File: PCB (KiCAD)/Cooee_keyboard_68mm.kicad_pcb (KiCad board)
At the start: 2 copper layers, 67.9 x 51 mm, 99 parts, among them J1 Conn_01x15_Pin

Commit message: finished routing new smaller keyboard
finished routing new smaller keyboard
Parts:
- removed H1: MountingHole, MountingHole:MountingHole_3.2mm_M3_ISO7380_Pad
- H4, H5: footprint MountingHole:MountingHole_3.2mm_M3_ISO7380_Pad -> MountingHole:MountingHole_3.2mm_M3
- moved D22 6.88 mm to (160.5, 120.5), turned to -90 degrees
- moved D93 6.28 mm to (161.1, 115.7), turned to -90 degrees
- moved J1 6.03 mm to (167.7, 73.2)
- moved D54 4.81 mm to (176.3, 111.8), turned to -90 degrees
- moved D18 4.56 mm to (157.8, 118.4)
- moved H4 4.52 mm to (177.2, 74.8)
- moved SWe7 3.32 mm to (171.0, 121.1)
- moved D28 3.27 mm to (170.4, 118.4)
- moved SWe13 2.74 mm to (157.0, 121.1)
- moved H5 2.58 mm to (121.8, 74.8)
- moved SWe2 1.84 mm to (163.8, 121.3), turned to 180 degrees
- moved SWe88 0.70 mm to (163.7, 115.0)
- moved H7 0.53 mm to (179.5, 119.0)
- moved D44 0.30 mm to (181.8, 89.4)
- moved SWe37 0.30 mm to (181.1, 86.8)
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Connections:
- D14 pad 1: COL2 -> COL3
- D17 pad 1: COL3 -> COL4
- D21 pad 1: COL4 -> COL5
- D22 pad 1: COL5 -> COL6
- D27 pad 1: COL6 -> COL7
- D28 pad 2: COL7 -> COL8
- D31 pad 1: COL7 -> COL8
- D39 pad 1: COL9 -> COL10
- D44 pad 1: COL9 -> COL10
- D5 pad 1: COL2 -> COL1
- D51 pad 1: COL8 -> COL2
- D52 pad 1: COL8 -> COL9
- D54 pad 1: COL8 -> COL10
- D7 pad 1: COL1 -> COL2
- D92 pad 1: COL5 -> COL6
- D93 pad 1: COL6 -> COL7
- J1 pad 1: ROW6 -> COL10
- J1 pad 2: ROW5 -> COL9
- J1 pad 3: ROW4 -> COL8
- J1 pad 4: ROW3 -> COL7
- J1 pad 5: ROW2 -> ROW5
- J1 pad 6: ROW1 -> ROW4
- J1 pad 7: COL9 -> ROW3
- J1 pad 8: COL8 -> ROW2
- J1 pad 9: COL7 -> ROW1
- SWe17 pad 1: ROW5 -> ROW4
- SWe2 pad 1: ROW6 -> ROW5
- SWe24 pad 1: ROW5 -> ROW4
- SWe29 pad 1: ROW2 -> ROW1
- SWe36 pad 1: ROW3 -> ROW2
- SWe37 pad 1: ROW6 -> ROW2
- SWe39 pad 1: ROW4 -> ROW3
- SWe47 pad 1: ROW4 -> ROW5
- SWe50 pad 1: ROW6 -> ROW5
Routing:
- net ROW5: track 0.00 -> 136.3 mm, vias 0 -> 1
- net ROW4: track 0.00 -> 103.9 mm, vias 0 -> 1
- net ROW3: track 0.00 -> 94.2 mm, vias 0 -> 1
- net ROW2: track 0.00 -> 89.4 mm, vias 0 -> 1
- net ROW1: track 0.00 -> 82.2 mm
- net COL6: track 0.00 -> 72.7 mm, vias 0 -> 5
- net COL8: track 0.00 -> 67.3 mm, vias 0 -> 5
- net COL5: track 0.00 -> 66.8 mm, vias 0 -> 5
- net COL1: track 0.00 -> 65.2 mm, vias 0 -> 5
- net COL9: track 0.00 -> 64.9 mm, vias 0 -> 5
- net COL2: track 0.00 -> 59.6 mm, vias 0 -> 5
- net COL10: track 0.00 -> 57.0 mm, vias 0 -> 3
- net COL7: track 0.00 -> 56.6 mm, vias 0 -> 5
- net COL4: track 0.00 -> 54.4 mm, vias 0 -> 4
- net COL3: track 0.00 -> 43.9 mm, vias 0 -> 4
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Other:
- board size 67.9 x 51 mm -> 66.8 x 51.8 mm

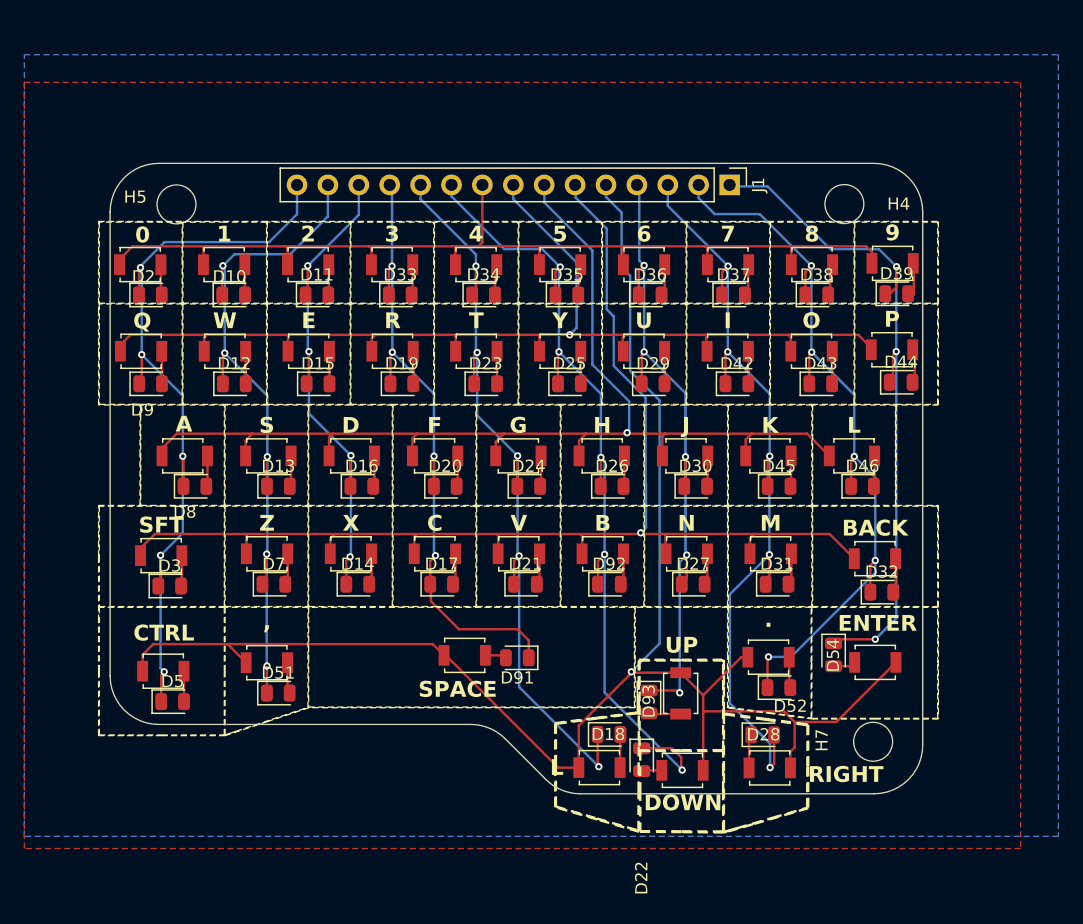
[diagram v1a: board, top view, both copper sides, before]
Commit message: finished keyboard at 67mm
started work on esp32 motherboard
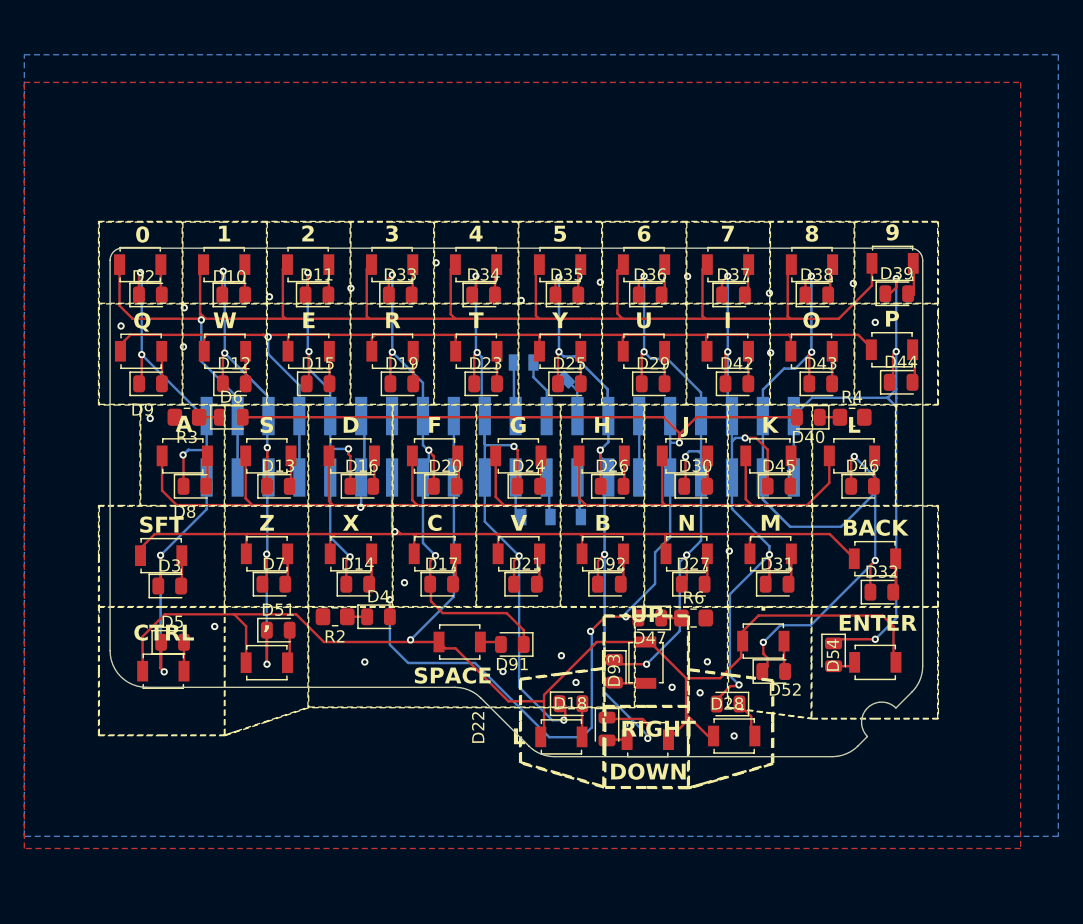
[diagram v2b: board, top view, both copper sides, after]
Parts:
- removed H4, H5, H7: MountingHole, MountingHole:MountingHole_3.2mm_M3
- added D4: SS24, Diode_SMD:D_0805_2012Metric, F.Cu at (138.9, 108.7)
- added D40: SS24, Diode_SMD:D_0805_2012Metric, F.Cu at (174.2, 92.3)
- added D47: SS24, Diode_SMD:D_0805_2012Metric, F.Cu at (161.2, 108.8)
- added D6: SS24, Diode_SMD:D_0805_2012Metric, F.Cu at (126.8, 92.3)
- added J2: Conn_01x01_Pin, USB4105-GF-A (1):Lil_Pad, B.Cu at (155.5, 100.5)
- added J3: Conn_01x01_Pin, USB4105-GF-A (1):Lil_Pad, B.Cu at (154.3, 89.2)
- added J4: Conn_01x01_Pin, USB4105-GF-A (1):Lil_Pad, B.Cu at (153.0, 100.5)
- added J5: Conn_01x01_Pin, USB4105-GF-A (1):Lil_Pad, B.Cu at (151.6, 87.8)
- added J6: Conn_01x01_Pin, USB4105-GF-A (1):Lil_Pad, B.Cu at (150.6, 100.5)
- added J7: Conn_01x01_Pin, USB4105-GF-A (1):Lil_Pad, B.Cu at (150.0, 87.8)
- added R2: R, Resistor_SMD:R_0805_2012Metric_Pad1.20x1.40mm_HandSolder, F.Cu at (135.3, 108.7)
- added R3: R, Resistor_SMD:R_0805_2012Metric_Pad1.20x1.40mm_HandSolder, F.Cu at (123.1, 92.3)
- added R4: R, Resistor_SMD:R_0805_2012Metric_Pad1.20x1.40mm_HandSolder, F.Cu at (177.8, 92.3)
- added R6: R, Resistor_SMD:R_0805_2012Metric_Pad1.20x1.40mm_HandSolder, F.Cu at (164.8, 108.8)
- J1: value Conn_01x15_Pin -> Conn_02x20_Counter_Clockwise; footprint Connector_PinHeader_2.54mm:PinHeader_1x15_P2.54mm_Vertical -> Connector_PinHeader_2.54mm:PinHeader_2x20_P2.54mm_Vertical_SMD; moved to B.Cu
- moved J1 28.6 mm to (148.9, 94.7)
- moved D51 5.17 mm to (130.6, 109.8)
- moved D5 4.88 mm to (121.9, 110.8)
- moved D18 4.02 mm to (154.7, 115.8)
- moved SWe13 4.02 mm to (153.9, 118.6)
- moved SWe7 3.93 mm to (168.1, 118.5), turned to 180 degrees
- moved D28 3.81 mm to (167.6, 115.9), turned to 180 degrees
- moved D22 3.81 mm to (157.7, 117.9)
- moved D93 3.81 mm to (158.3, 113.2)
- moved SWe2 3.81 mm to (161.0, 118.8)
- moved SWe88 3.81 mm to (160.9, 112.5)
- moved SWe48 1.39 mm to (170.5, 110.7)
- moved D52 1.39 mm to (171.4, 113.2)
- moved D91 1.17 mm to (149.9, 111.0)
- moved SWe86 1.17 mm to (145.5, 110.8)
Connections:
- J1 pad 1: COL10 -> COL1
- J1 pad 10: COL6 -> COL3
- J1 pad 11: COL5 -> ROW3
- J1 pad 12: COL4 -> ROW3
- J1 pad 13: COL3 -> ROW4
- J1 pad 14: COL2 -> ROW4
- J1 pad 15: COL1 -> COL4
- J1 pad 2: COL9 -> COL1
- J1 pad 3: COL8 -> ROW1
- J1 pad 4: COL7 -> ROW1
- J1 pad 5: ROW5 -> COL2
- J1 pad 6: ROW4 -> COL2
- J1 pad 7: ROW3 -> ROW2
- J1 pad 9: ROW1 -> COL3
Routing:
- net +3.3V: track 0.00 -> 104.5 mm, vias 0 -> 4
- net ROW1: track 82.2 -> 122.4 mm, vias 0 -> 1
- net ROW5: track 136.3 -> 115.3 mm
- net ROW4: track 103.9 -> 83.0 mm
- net COL6: track 72.7 -> 57.2 mm
- net COL8: track 67.3 -> 53.2 mm
- net COL2: track 59.6 -> 47.2 mm
- net COL1: track 65.2 -> 52.9 mm
- net COL5: track 66.8 -> 56.8 mm
- net COL4: track 54.4 -> 46.3 mm
- net COL7: track 56.6 -> 50.6 mm
- net COL3: track 43.9 -> 38.1 mm
- net ROW3: track 94.2 -> 99.7 mm
- net GND: track 0.00 -> 5.15 mm, vias 0 -> 25
- net SPARE4: track 0.00 -> 4.86 mm
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- added copper zone on B.Cu, net GND
- added copper zone on F.Cu, net GND
- removed copper zone on B.Cu, net (none)
- removed copper zone on F.Cu, net (none)
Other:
- board size 66.8 x 51.8 mm -> 66.8 x 41.8 mm

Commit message: cleaned up the silkscreen for keyboard PCB
cleaned up the silkscreen for keyboard PCB, ordered prototypes
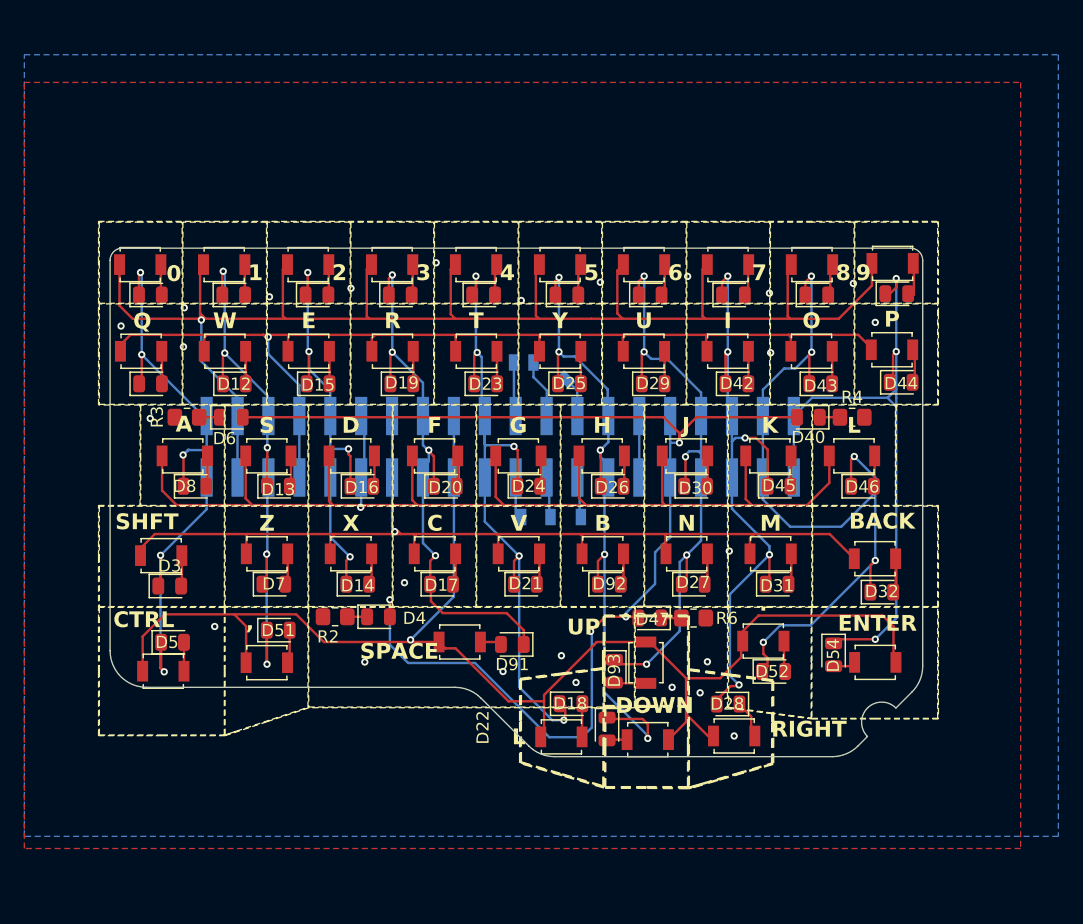
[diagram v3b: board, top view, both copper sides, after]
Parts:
- SWe24: value SFT -> SHFT
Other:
- board text added: "+"
- board text added: "-"
- board text added: "3.3V LEDs"
- board text added: "Col 1"
- board text added: "Col 10"
- board text added: "Col 2"
- board text added: "Col 3"
- board text added: "Col 4"
- board text added: "Col 5"
- board text added: "Col 6"
- board text added: "Col 7"
- board text added: "Col 8"
- board text added: "Col 9"
- board text added: "GROUND"
- board text added: "Row 1"
- board text added: "Row 2"
- board text added: "Row 3"
- board text added: "Row 4"
- board text added: "Row 5"

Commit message: more PCB work
should have the 90 degree SMD header pins lined up to mount now, unfortunately I've invalidated the keyboard prototypes I already bought
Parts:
- removed J1: Conn_02x20_Counter_Clockwise, Connector_PinHeader_2.54mm:PinHeader_2x20_P2.54mm_Vertical_SMD
- removed J3, J4, J5, J6, J7: Conn_01x01_Pin, USB4105-GF-A (1):Lil_Pad
- added J99: Conn_01x18_Socket, USB4105-GF-A (1):SMD_Header_1x18_P2.54mm, B.Cu at (146.3, 91.7)
- SWe24: value SHFT -> SFT
- moved J2 0.38 mm to (155.2, 100.2)
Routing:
- net COL8: track 53.2 -> 67.9 mm
- net COL10: track 53.9 -> 64.1 mm
- net COL9: track 65.6 -> 71.3 mm
- net ROW1: track 122.4 -> 117.3 mm
- net SPARE4: track 4.86 -> 0.00 mm
- net GND: track 5.15 -> 0.30 mm, vias 25 -> 33
- net SPARE6: track 4.46 -> 0.00 mm
- net SPARE5: track 3.94 -> 0.00 mm
- net SPARE3: track 3.88 -> 0.00 mm
- net SPARE1: track 3.87 -> 7.62 mm
- net SPARE2: track 3.38 -> 0.00 mm
- net +3.3V: track 104.5 -> 105.9 mm, vias 4 -> 3
- net COL3: track 38.1 -> 39.2 mm
- net COL7: track 50.6 -> 49.7 mm, vias 5 -> 6

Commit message: new IC choices for GPS, audio and power
also added a keyboard IC to the keyboard to preventing wasting precious ESP32 GPIOs
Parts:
- removed J2: Conn_01x01_Pin, USB4105-GF-A (1):Lil_Pad
- removed J99: Conn_01x18_Socket, USB4105-GF-A (1):SMD_Header_1x18_P2.54mm
- added R1: 10k, Resistor_SMD:R_0805_2012Metric_Pad1.20x1.40mm_HandSolder, F.Cu at (147.5, 115.8)
- added R5: 10k, Resistor_SMD:R_0805_2012Metric_Pad1.20x1.40mm_HandSolder, F.Cu at (147.5, 117.8)
- added U1: TCA8418RTWR, USB4105-GF-A (1):QFN50P400X400X100-25N, F.Cu at (141.3, 115.3)
- R2, R3, R4, R6: value R -> 1000
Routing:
- net COL10: track 64.1 -> 45.0 mm, vias 3 -> 4
- net COL9: track 71.3 -> 53.9 mm, vias 5 -> 6
- net ROW5: track 115.3 -> 98.3 mm, vias 1 -> 2
- net COL1: track 52.9 -> 64.9 mm, vias 5 -> 6
- net +3.3V: track 105.9 -> 117.5 mm, vias 3 -> 4
- net ROW2: track 87.8 -> 76.8 mm
- net ROW4: track 83.0 -> 73.4 mm, vias 1 -> 0
- net ROW1: track 117.3 -> 110.5 mm
- net ROW3: track 99.7 -> 93.5 mm
- net KEEB_SCL: track 0.00 -> 5.92 mm
- net KEEB_D: track 0.00 -> 5.73 mm
- net COL6: track 57.2 -> 52.6 mm, vias 5 -> 6
- net COL7: track 49.7 -> 54.2 mm, vias 6 -> 7
- net SPARE1: track 7.62 -> 3.51 mm, vias 0 -> 1
- net unconnected-(U1-ROW5-Pad3): track 0.00 -> 3.72 mm, vias 0 -> 1
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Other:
- outline, holes or cut-outs redrawn

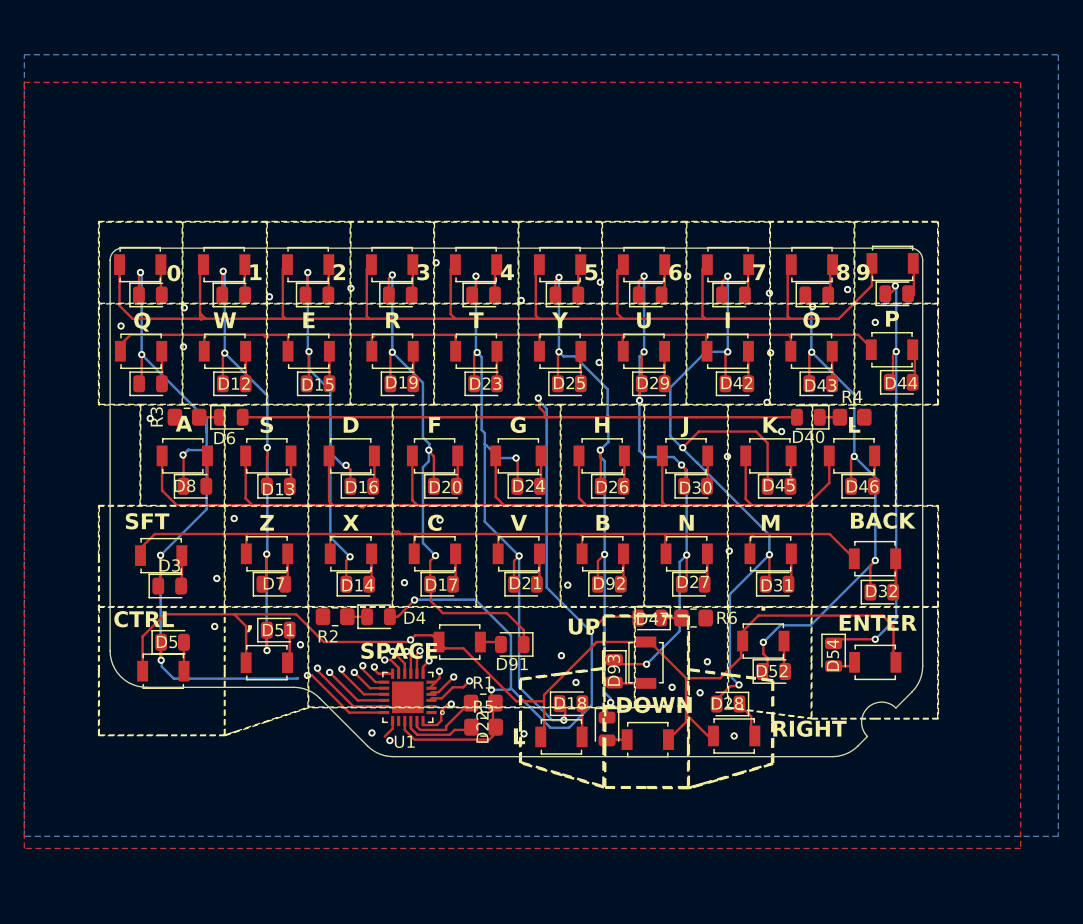
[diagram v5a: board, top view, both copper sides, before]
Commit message: finalized next prototype of keyboard PCB, ready to order
finalized next prototype of keyboard PCB, ready to order
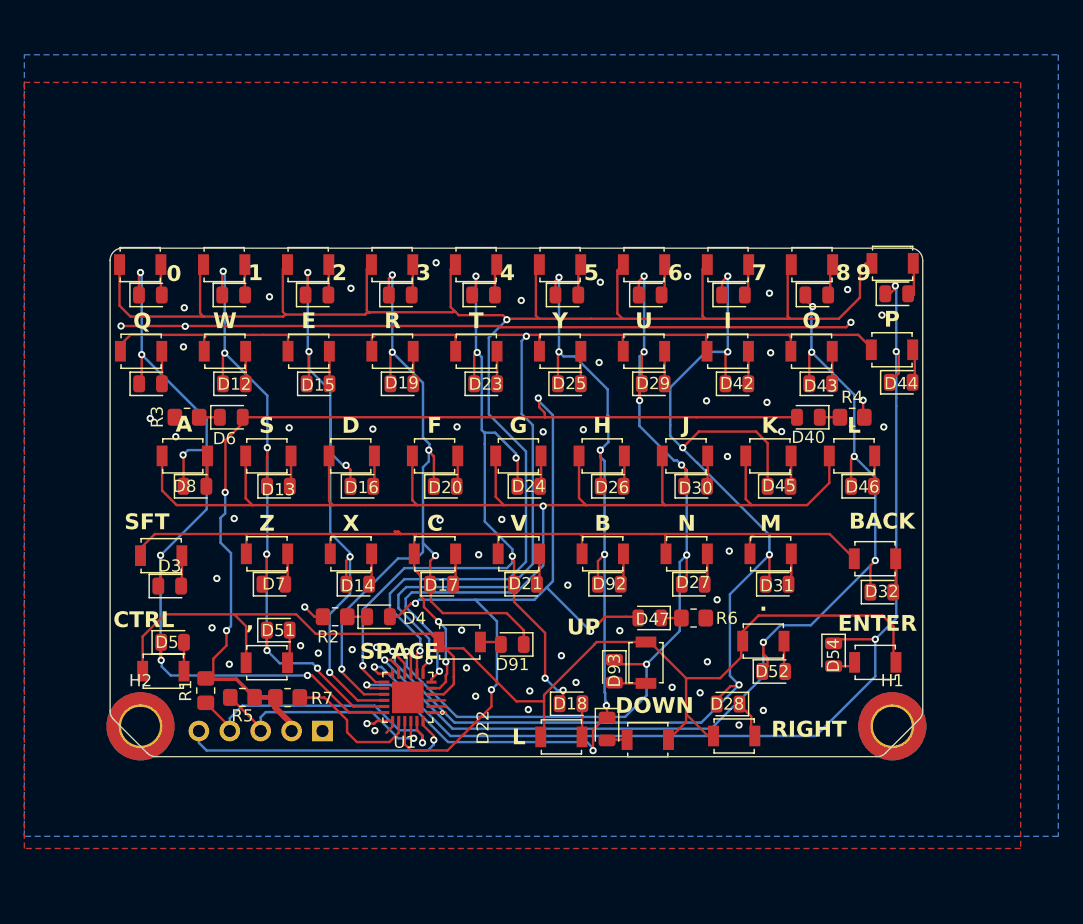
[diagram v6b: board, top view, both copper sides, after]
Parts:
- added H1: MountingHole_Pad, MountingHole:MountingHole_3.2mm_M3_DIN965_Pad_TopBottom, F.Cu at (181.1, 117.7)
- added H2: MountingHole_Pad, MountingHole:MountingHole_3.2mm_M3_DIN965_Pad_TopBottom, F.Cu at (119.3, 117.7)
- added J9: Conn_01x05_Pin, Connector_PinHeader_2.54mm:PinHeader_1x05_P2.54mm_Horizontal, B.Cu at (134.3, 118.1)
- added R7: 10k, Resistor_SMD:R_0805_2012Metric_Pad1.20x1.40mm_HandSolder, F.Cu at (131.4, 115.3)
- moved R1 22.8 mm to (124.7, 114.8), turned to 90 degrees
- moved R5 20.0 mm to (127.7, 115.3)
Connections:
- D10 pad 1: COL2 -> COL9
- D11 pad 1: COL3 -> COL8
- D12 pad 1: COL2 -> COL9
- D13 pad 1: COL2 -> COL9
- D14 pad 1: COL3 -> COL8
- D15 pad 1: COL3 -> COL8
- D16 pad 1: COL3 -> COL8
- D17 pad 1: COL4 -> COL7
- D19 pad 1: COL4 -> COL7
- D2 pad 1: COL1 -> COL10
- D20 pad 1: COL4 -> COL7
- D27 pad 1: COL7 -> COL4
- D28 pad 2: COL8 -> COL3
- D29 pad 1: COL7 -> COL4
- D3 pad 1: COL1 -> COL10
- D30 pad 1: COL7 -> COL4
- D31 pad 1: COL8 -> COL3
- D32 pad 1: COL9 -> COL2
- D33 pad 1: COL4 -> COL7
- D36 pad 1: COL7 -> COL4
- D37 pad 1: COL8 -> COL3
- D38 pad 1: COL9 -> COL2
- D39 pad 1: COL10 -> COL1
- D42 pad 1: COL8 -> COL3
- D43 pad 1: COL9 -> COL2
- D44 pad 1: COL10 -> COL1
- D45 pad 1: COL8 -> COL3
- D46 pad 1: COL9 -> COL2
- D5 pad 1: COL1 -> COL10
- D51 pad 1: COL2 -> COL9
- D52 pad 1: COL9 -> COL2
- D54 pad 1: COL10 -> COL1
- D7 pad 1: COL2 -> COL9
- D8 pad 1: COL1 -> COL10
- D9 pad 1: COL1 -> COL10
- D91 pad 1: COL4 -> COL7
- D93 pad 1: COL7 -> COL4
- U1 pad 10: COL2 -> COL3
- U1 pad 11: COL3 -> COL2
- U1 pad 12: COL4 -> COL1
- U1 pad 20: KEEP_RST -> KEEB_RST
- U1 pad 24: SPARE1 -> KEEB_INT
- U1 pad 9: COL1 -> COL4
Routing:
- net GND: track 1.32 -> 67.0 mm, vias 35 -> 59
- net COL3: track 41.4 -> 98.9 mm, vias 5 -> 6
- net COL2: track 47.3 -> 87.3 mm
- net ROW1: track 110.5 -> 148.7 mm, vias 1 -> 2
- net ROW2: track 76.8 -> 114.1 mm, vias 1 -> 2
- net COL4: track 48.2 -> 76.8 mm, vias 5 -> 7
- net COL10: track 45.0 -> 69.4 mm, vias 4 -> 6
- net KEEB_INT: track 0.00 -> 23.7 mm, vias 0 -> 1
- net ROW3: track 93.5 -> 117.1 mm, vias 1 -> 2
- net COL1: track 64.9 -> 88.1 mm, vias 6 -> 4
- net +3.3V: track 117.5 -> 140.1 mm, vias 4 -> 6
- net COL6: track 52.6 -> 74.7 mm, vias 6 -> 7
- net KEEB_SCL: track 5.92 -> 24.3 mm, vias 0 -> 1
- net KEEB_D: track 5.73 -> 20.1 mm, vias 0 -> 1
- net COL8: track 69.1 -> 54.8 mm, vias 6 -> 5
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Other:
- outline, holes or cut-outs redrawn
- board text added: "+3.3V"
- board text added: "CLOCK"
- board text added: "COOEE"
- board text added: "DATA"
- board text added: "Keyboard designed for the Cooee project"
- board text added: "Visit: Github.com/DetectiveMittens/Cooee/"
- board text added: "~INT"
- board text removed: "3.3V LEDs"
- board text removed: "Col 1"
- board text removed: "Col 10"
- board text removed: "Col 2"
- board text removed: "Col 3"
- board text removed: "Col 4"
- board text removed: "Col 5"
- board text removed: "Col 6"
- board text removed: "Col 7"
- board text removed: "Col 8"
- board text removed: "Col 9"
- board text removed: "Row 1"
- board text removed: "Row 2"
- board text removed: "Row 3"
- board text removed: "Row 4"
- board text removed: "Row 5"
